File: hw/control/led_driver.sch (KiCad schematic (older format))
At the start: 7 parts, among them U1101 SN74AHCT125D

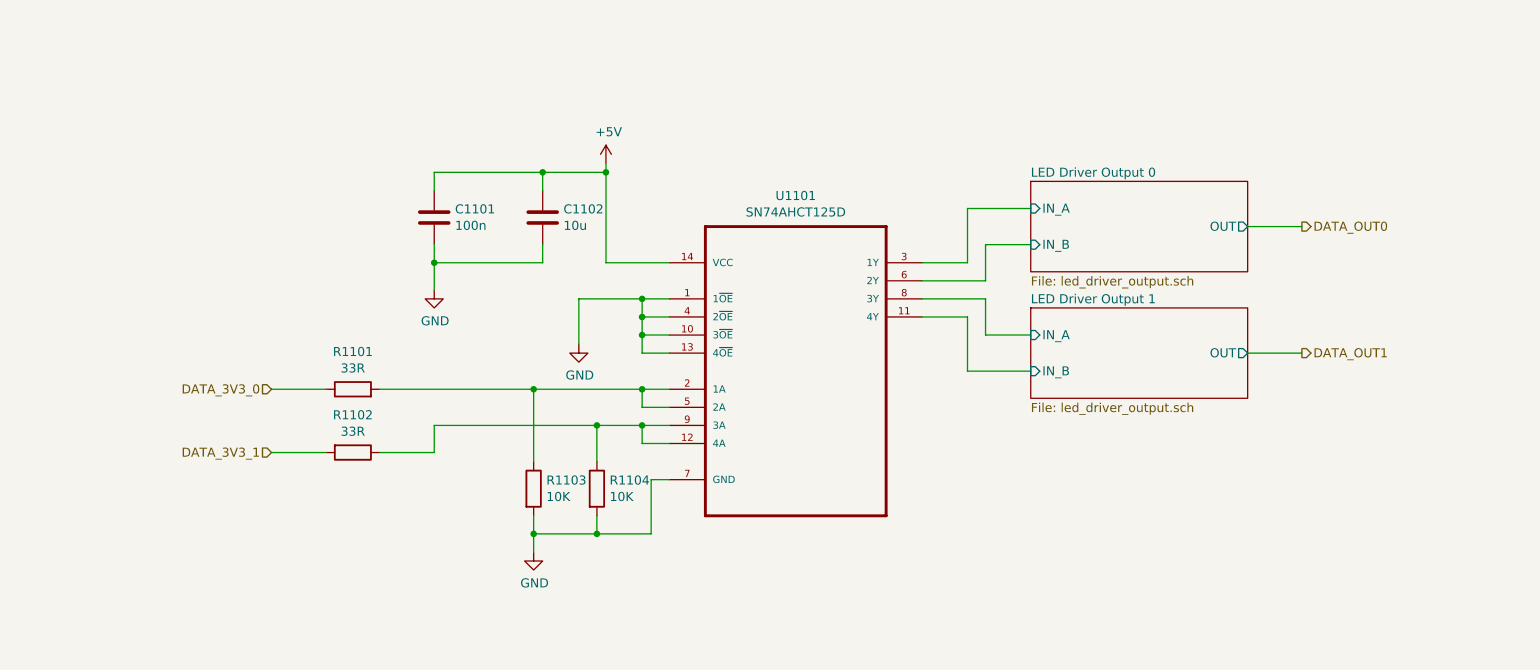
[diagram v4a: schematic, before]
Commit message: [hw] Add alternative LED data line from SPI
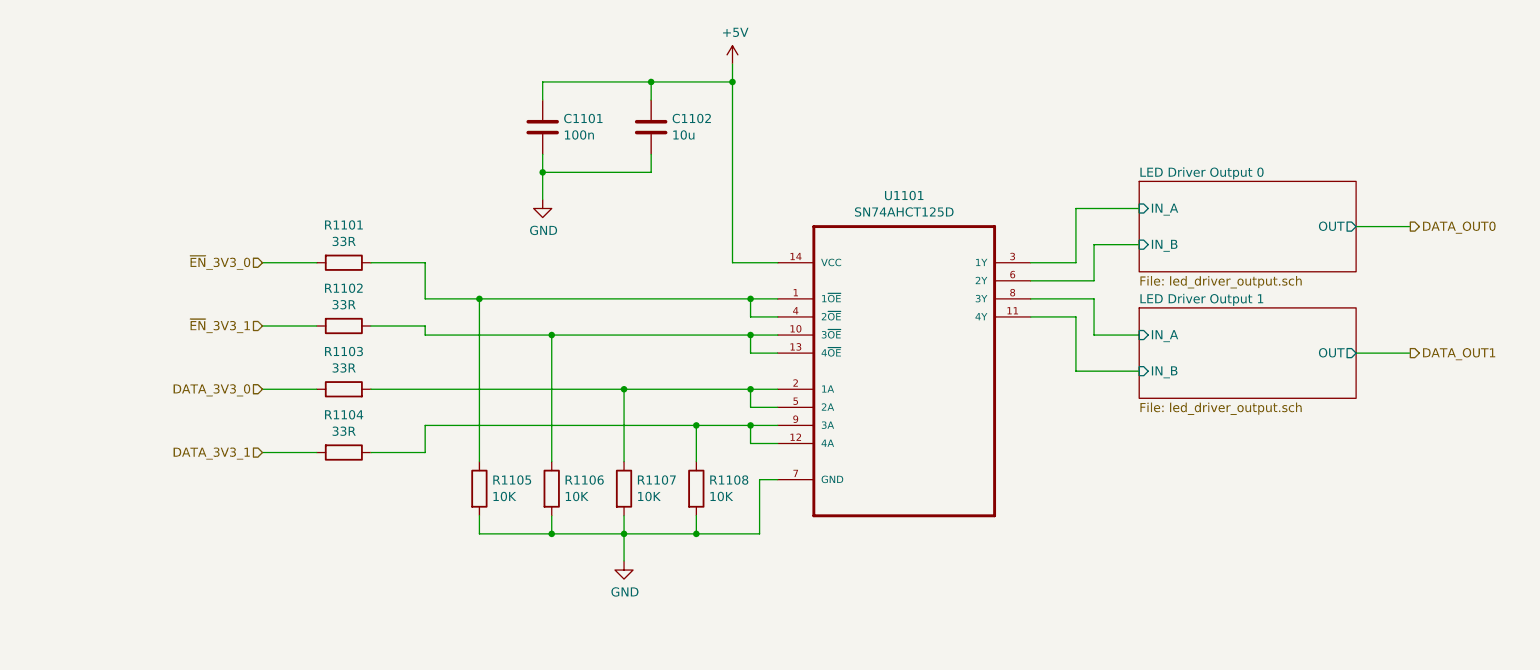
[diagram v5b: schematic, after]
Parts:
- added R1101, R1102: 33R, symbol Device:R
- added R1105, R1106: 10K, symbol Device:R
- renumbered R1101 to R1103, R1102 to R1104, R1103 to R1107, R1104 to R1108
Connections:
- net GND: now also R1105.2, R1106.2; no longer U1101.1 (1~OE), U1101.10 (3~OE), U1101.13 (4~OE), U1101.4 (2~OE)
- new net: R1101.1, R1105.1, U1101.1 (1~OE), U1101.4 (2~OE)
- new net: R1102.1, R1106.1, U1101.10 (3~OE), U1101.13 (4~OE)
- new net ~EN~_3V3_0: R1101.2
- new net ~EN~_3V3_1: R1102.2
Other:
- moved on the sheet: C1101, C1102, R1103, R1104, R1107, R1108, U1101

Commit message: [hw] Assign most of the controller footprints
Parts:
- C1101: footprint (none) -> Capacitor_SMD:C_0805_2012Metric_Pad1.18x1.45mm_HandSolder
- R1101, R1102, R1103, R1104, R1105, R1106, R1107, R1108: footprint (none) -> Resistor_SMD:R_0805_2012Metric_Pad1.20x1.40mm_HandSolder
- U1101: footprint SOIC127P600X175-14N -> Package_SO:SO-14_3.9x8.65mm_P1.27mm
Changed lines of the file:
@@
 F 0 "U1101" H 6300 4820 50  0000 C CNN
 F 1 "SN74AHCT125D" H 6300 4729 50  0000 C CNN
-F 2 "SOIC127P600X175-14N" H 6300 3950 50  0001 L BNN
+F 2 "Package_SO:SO-14_3.9x8.65mm_P1.27mm" H 6300 3950 50  0001 L BNN
 F 3 "SOIC-14 Texas Instruments" H 6300 3950 50  0001 L BNN
 F 4 "Buffer-line Driver 4 Channel Non-Inverting 3 State CMOS 14-Pin SOIC Tube" H 6300 3950 50  0001 L BNN "Field4"
@@
 F 0 "C1101" H 4415 2746 50  0000 L CNN
 F 1 "100n" H 4415 2655 50  0000 L CNN
-F 2 "" H 4338 2550 50  0001 C CNN
+F 2 "Capacitor_SMD:C_0805_2012Metric_Pad1.18x1.45mm_HandSolder" H 4338 2550 50  0001 C CNN
 F 3 "~" H 4300 2700 50  0001 C CNN
 	1    4300 2700
@@
 F 0 "R1108" H 5220 4746 50  0000 L CNN
 F 1 "10K" H 5220 4655 50  0000 L CNN
-F 2 "" V 5080 4700 50  0001 C CNN
+F 2 "Resistor_SMD:R_0805_2012Metric_Pad1.20x1.40mm_HandSolder" V 5080 4700 50  0001 C CNN
 F 3 "~" H 5150 4700 50  0001 C CNN
 	1    5150 4700
@@
 F 0 "R1107" H 4820 4746 50  0000 L CNN
 F 1 "10K" H 4820 4655 50  0000 L CNN
-F 2 "" V 4680 4700 50  0001 C CNN
+F 2 "Resistor_SMD:R_0805_2012Metric_Pad1.20x1.40mm_HandSolder" V 4680 4700 50  0001 C CNN
 F 3 "~" H 4750 4700 50  0001 C CNN
 	1    4750 4700
@@
 F 0 "R1103" V 3407 4150 50  0000 C CNN
 F 1 "33R" V 3316 4150 50  0000 C CNN
-F 2 "" V 3130 4150 50  0001 C CNN
+F 2 "Resistor_SMD:R_0805_2012Metric_Pad1.20x1.40mm_HandSolder" V 3130 4150 50  0001 C CNN
 F 3 "~" H 3200 4150 50  0001 C CNN
 	1    3200 4150
@@
 F 0 "R1104" V 2993 4500 50  0000 C CNN
 F 1 "33R" V 3084 4500 50  0000 C CNN
-F 2 "" V 3130 4500 50  0001 C CNN
+F 2 "Resistor_SMD:R_0805_2012Metric_Pad1.20x1.40mm_HandSolder" V 3130 4500 50  0001 C CNN
 F 3 "~" H 3200 4500 50  0001 C CNN
 	1    3200 4500
@@
 F 0 "R1102" V 2993 3800 50  0000 C CNN
 F 1 "33R" V 3084 3800 50  0000 C CNN
-F 2 "" V 3130 3800 50  0001 C CNN
+F 2 "Resistor_SMD:R_0805_2012Metric_Pad1.20x1.40mm_HandSolder" V 3130 3800 50  0001 C CNN
 F 3 "~" H 3200 3800 50  0001 C CNN
 	1    3200 3800
@@
 F 0 "R1101" V 2993 3450 50  0000 C CNN
 F 1 "33R" V 3084 3450 50  0000 C CNN
-F 2 "" V 3130 3450 50  0001 C CNN
+F 2 "Resistor_SMD:R_0805_2012Metric_Pad1.20x1.40mm_HandSolder" V 3130 3450 50  0001 C CNN
 F 3 "~" H 3200 3450 50  0001 C CNN
 	1    3200 3450
@@
 F 0 "R1106" H 4420 4746 50  0000 L CNN
 F 1 "10K" H 4420 4655 50  0000 L CNN
-F 2 "" V 4280 4700 50  0001 C CNN
+F 2 "Resistor_SMD:R_0805_2012Metric_Pad1.20x1.40mm_HandSolder" V 4280 4700 50  0001 C CNN
 F 3 "~" H 4350 4700 50  0001 C CNN
 	1    4350 4700
@@
 F 0 "R1105" H 4020 4746 50  0000 L CNN
 F 1 "10K" H 4020 4655 50  0000 L CNN
-F 2 "" V 3880 4700 50  0001 C CNN
+F 2 "Resistor_SMD:R_0805_2012Metric_Pad1.20x1.40mm_HandSolder" V 3880 4700 50  0001 C CNN
 F 3 "~" H 3950 4700 50  0001 C CNN
 	1    3950 4700

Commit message: [hw] Assign control board footprints
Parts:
- C1102: footprint (none) -> Capacitor_SMD:C_1206_3216Metric_Pad1.33x1.80mm_HandSolder
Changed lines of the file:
@@
 F 0 "C1102" H 5015 2746 50  0000 L CNN
 F 1 "10u" H 5015 2655 50  0000 L CNN
-F 2 "" H 4938 2550 50  0001 C CNN
+F 2 "Capacitor_SMD:C_1206_3216Metric_Pad1.33x1.80mm_HandSolder" H 4938 2550 50  0001 C CNN
 F 3 "~" H 4900 2700 50  0001 C CNN
 	1    4900 2700
